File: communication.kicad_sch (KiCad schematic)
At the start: 12 parts, among them IC10 nRF52832-QFAA-R7, Y1 32Mhz

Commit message: added footprint for nRF, changed symbol background color, checked connections
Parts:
- removed IC10: nRF52832-QFAA-R7, QFN40P600X600X90-49N-D, symbol ARMband:nRF52832-QFAA-R7
- added IC11: nRF52832-QFAA-R7, QFN40P600X600X90-49N-D, symbol ARMband:nRF52832-QFAA-R7
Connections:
- net ANT: now also IC11.30 (ANT)
- net BUCK4_1V8: now also IC11.13 (VDD_1), IC11.36 (VDD_2), IC11.48 (VDD_3)
- net DCC: now also IC11.47 (DCC)
- net DEC4: now also IC11.46 (DEC4)
- net GND: now also IC11.31 (VSS_1), IC11.45 (VSS_2), IC11.49 (THERMAL_PAD)
- net nRF_XC1: now also IC11.34 (XC1)
- net nRF_XC2: now also IC11.35 (XC2)
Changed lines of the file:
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@@
     )
   )
-  (symbol (lib_id "ARMband:nRF52832-QFAA-R7") (at 43.18 73.66 0) (unit 1)
+  (symbol (lib_id "Device:L_Small") (at 121.92 69.85 90) (unit 1)
     (in_bom yes) (on_board yes) (dnp no) (fields_autoplaced)
-    (property "Reference" "IC10" (at 57.8359 136.2917 0)
+    (property "Reference" "L8" (at 121.92 66.4613 90)
+      (effects (font (size 1.27 1.27)))
+    )
+    (property "Value" "3.9nH" (at 121.92 68.3823 90)
+      (effects (font (size 1.27 1.27)))
+    )
+    (property "Footprint" "" (at 121.92 69.85 0)
+      (effects (font (size 1.27 1.27)) hide)
+    )
+    (property "Datasheet" "~" (at 121.92 69.85 0)
+      (effects (font (size 1.27 1.27)) hide)
+    )
+    (pin "1")
+    (pin "2")
+    (instances
+      (project "gba"
+        (path "/017c50c6-333c-4d31-ad5a-278994a09b14/647ca51e-1670-44f9-a82c-44b1c60d10f9"
+          (reference "L8") (unit 1)
+        )
+      )
+    )
+  )
+  (symbol (lib_id "Device:C_Small") (at 119.38 54.61 0) (unit 1)
+    (in_bom yes) (on_board yes) (dnp no)
+    (property "Reference" "C69" (at 125.73 55.88 0)
+      (effects (font (size 1.27 1.27)) (justify right))
+    )
+    (property "Value" "100nF" (at 125.73 53.34 0)
+      (effects (font (size 1.27 1.27)) (justify right))
+    )
+    (property "Footprint" "" (at 119.38 54.61 0)
+      (effects (font (size 1.27 1.27)) hide)
+    )
+    (property "Datasheet" "~" (at 119.38 54.61 0)
+      (effects (font (size 1.27 1.27)) hide)
+    )
+    (pin "1")
+    (pin "2")
+    (instances
+      (project "gba"
+        (path "/017c50c6-333c-4d31-ad5a-278994a09b14/647ca51e-1670-44f9-a82c-44b1c60d10f9"
+          (reference "C69") (unit 1)
+        )
+      )
+    )
+  )
+  (symbol (lib_id "Device:L_Small") (at 147.32 52.07 180) (unit 1)
+    (in_bom yes) (on_board yes) (dnp no) (fields_autoplaced)
+    (property "Reference" "L7" (at 147.955 51.4263 0)
+      (effects (font (size 1.27 1.27)) (justify right))
+    )
+    (property "Value" "10uH" (at 147.955 53.3473 0)
+      (effects (font (size 1.27 1.27)) (justify right))
+    )
+    (property "Footprint" "" (at 147.32 52.07 0)
+      (effects (font (size 1.27 1.27)) hide)
+    )
+    (property "Datasheet" "~" (at 147.32 52.07 0)
+      (effects (font (size 1.27 1.27)) hide)
+    )
+    (pin "1")
+    (pin "2")
+    (instances
+      (project "gba"
+        (path "/017c50c6-333c-4d31-ad5a-278994a09b14/647ca51e-1670-44f9-a82c-44b1c60d10f9"
+          (reference "L7") (unit 1)
+        )
+      )
+    )
+  )
+  (symbol (lib_name "nRF52832-QFAA-R7_1") (lib_id "ARMband:nRF52832-QFAA-R7") (at 43.18 73.66 0) (unit 1)
+    (in_bom yes) (on_board yes) (dnp no) (fields_autoplaced)
+    (property "Reference" "IC11" (at 57.8359 137.16 0)
       (effects (font (size 1.27 1.27)) (justify left))
     )
-    (property "Value" "nRF52832-QFAA-R7" (at 57.8359 138.2127 0)
+    (property "Value" "nRF52832-QFAA-R7" (at 57.8359 139.7 0)
       (effects (font (size 1.27 1.27)) (justify left))
     )
@@
       (project "gba"
         (path "/017c50c6-333c-4d31-ad5a-278994a09b14/647ca51e-1670-44f9-a82c-44b1c60d10f9"
-          (reference "IC10") (unit 1)
+          (reference "IC11") (unit 1)
         )
       )
-    )
-  )
-  (symbol (lib_id "Device:L_Small") (at 121.92 69.85 90) (unit 1)
-    (in_bom yes) (on_board yes) (dnp no) (fields_autoplaced)
-    (property "Reference" "L8" (at 121.92 66.4613 90)
-      (effects (font (size 1.27 1.27)))
-    )
-    (property "Value" "3.9nH" (at 121.92 68.3823 90)
-      (effects (font (size 1.27 1.27)))
-    )
-    (property "Footprint" "" (at 121.92 69.85 0)
-      (effects (font (size 1.27 1.27)) hide)
-    )
-    (property "Datasheet" "~" (at 121.92 69.85 0)
-      (effects (font (size 1.27 1.27)) hide)
-    )
-    (pin "1")
-    (pin "2")
-    (instances
-      (project "gba"
-        (path "/017c50c6-333c-4d31-ad5a-278994a09b14/647ca51e-1670-44f9-a82c-44b1c60d10f9"
-          (reference "L8") (unit 1)
-        )
-      )
-    )
-  )
-  (symbol (lib_id "Device:C_Small") (at 119.38 54.61 0) (unit 1)
-    (in_bom yes) (on_board yes) (dnp no)
-    (property "Reference" "C69" (at 125.73 55.88 0)
-      (effects (font (size 1.27 1.27)) (justify right))
-    )
-    (property "Value" "100nF" (at 125.73 53.34 0)
-      (effects (font (size 1.27 1.27)) (justify right))
-    )
-    (property "Footprint" "" (at 119.38 54.61 0)
-      (effects (font (size 1.27 1.27)) hide)
-    )
-    (property "Datasheet" "~" (at 119.38 54.61 0)
-      (effects (font (size 1.27 1.27)) hide)
-    )
-    (pin "1")
-    (pin "2")
-    (instances
-      (project "gba"
-        (path "/017c50c6-333c-4d31-ad5a-278994a09b14/647ca51e-1670-44f9-a82c-44b1c60d10f9"
-          (reference "C69") (unit 1)
-        )
-      )
-    )
-  )
-  (symbol (lib_id "Device:L_Small") (at 147.32 52.07 180) (unit 1)
-    (in_bom yes) (on_board yes) (dnp no) (fields_autoplaced)
-    (property "Reference" "L7" (at 147.955 51.4263 0)
-      (effects (font (size 1.27 1.27)) (justify right))
-    )
-    (property "Value" "10uH" (at 147.955 53.3473 0)
-      (effects (font (size 1.27 1.27)) (justify right))
-    )
-    (property "Footprint" "" (at 147.32 52.07 0)
-      (effects (font (size 1.27 1.27)) hide)
-    )
-    (property "Datasheet" "~" (at 147.32 52.07 0)
-      (effects (font (size 1.27 1.27)) hide)
-    )
-    (pin "1")
-    (pin "2")
-    (instances
-      (project "gba"
-        (path "/017c50c6-333c-4d31-ad5a-278994a09b14/647ca51e-1670-44f9-a82c-44b1c60d10f9"
-          (reference "L7") (unit 1)
-        )
-      )

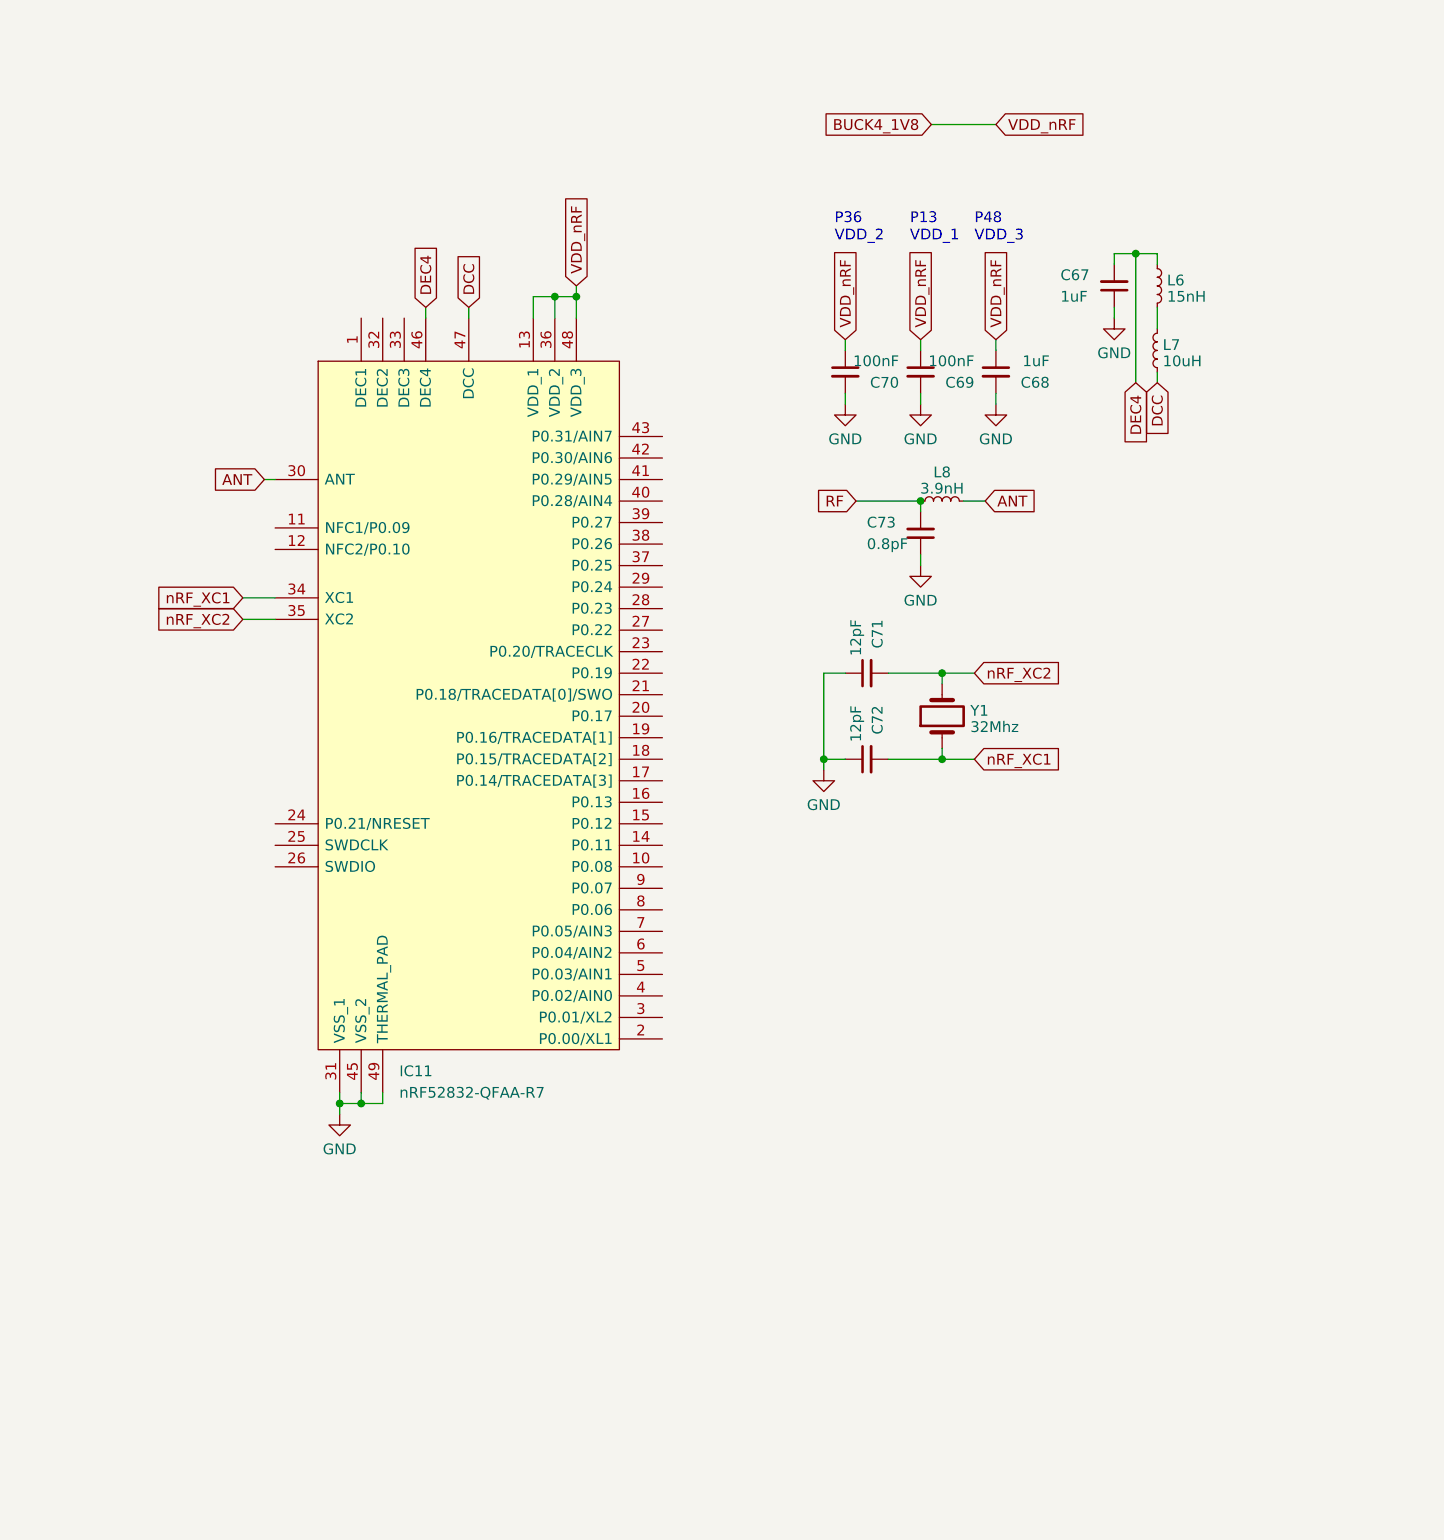
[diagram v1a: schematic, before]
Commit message: added supply to nRF
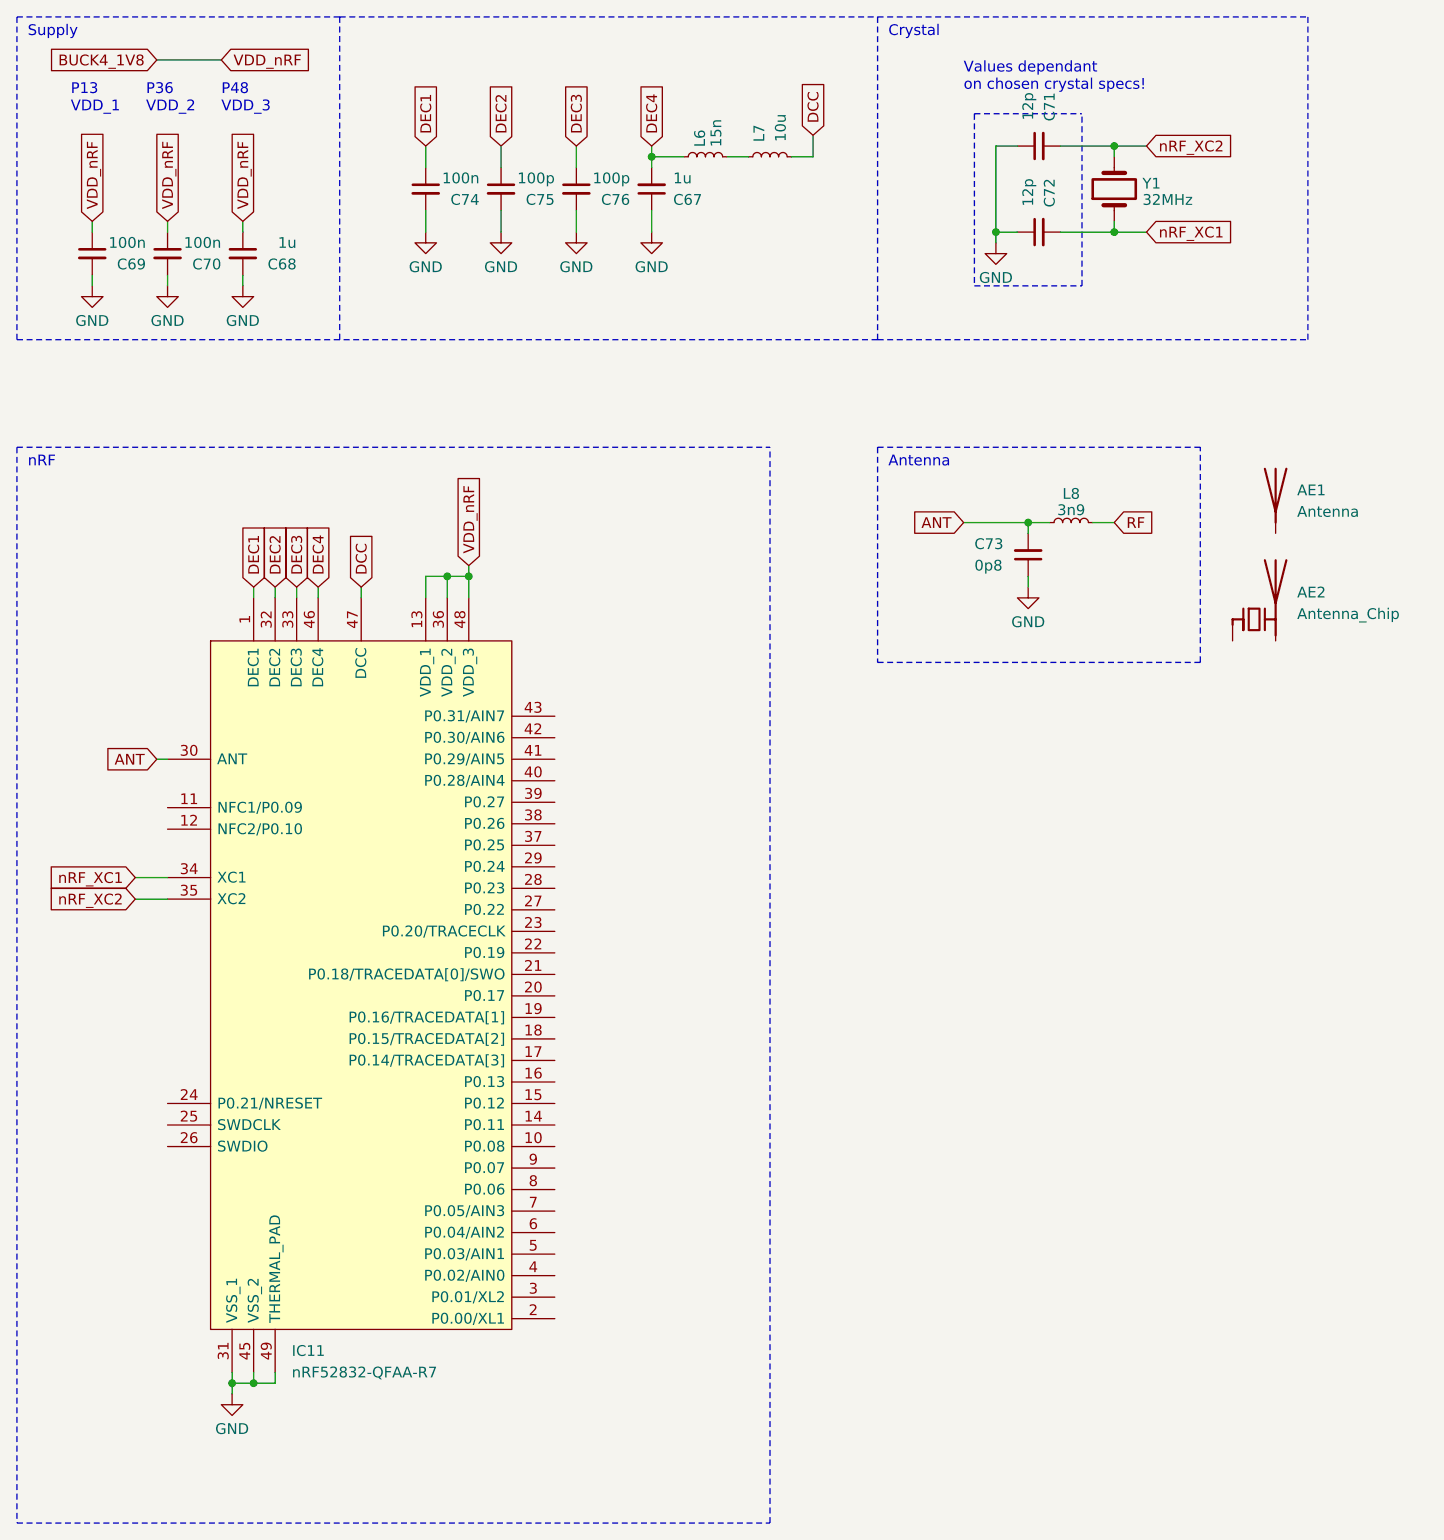
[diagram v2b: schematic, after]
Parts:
- added AE1: Antenna, symbol Device:Antenna
- added AE2: Antenna_Chip, symbol Device:Antenna_Chip
- added C74: 100n, symbol Device:C_Small
- added C75, C76: 100p, symbol Device:C_Small
- C67, C68: value 1uF -> 1u
- C69, C70: value 100nF -> 100n
- C71, C72: value 12pF -> 12p
- C73: value 0.8pF -> 0p8
- L6: value 15nH -> 15n
- L7: value 10uH -> 10u
- L8: value 3.9nH -> 3n9
- Y1: value 32Mhz -> 32MHz
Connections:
- net ANT: now also C73.2, L8.1; no longer L8.2
- net DCC: now also L7.2; no longer L7.1
- net GND: now also C74.2, C75.2, C76.2
- net RF: now also L8.2; no longer C73.2, L8.1
- net at L6.2: now also L7.1; no longer L7.2
- net DEC1: now reaches IC11.1 (DEC1)
- net DEC1: now also C74.1
- net DEC2: now reaches IC11.32 (DEC2)
- net DEC2: now also C75.1
- net DEC3: now reaches IC11.33 (DEC3)
- net DEC3: now also C76.1
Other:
- note added: "Antenna"
- note added: "Crystal"
- note added: "Supply"
- note added: "Values dependant on chosen crystal specs!"
- note added: "nRF"
- moved on the sheet: C67, C68, C69, C70, C71, C72, C73, IC11, L6, L7, L8, Y1

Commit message: added decoupling capacitors to mp1
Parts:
- C68: value 1u -> 4u7
- C75: now not fitted
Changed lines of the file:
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@@
       (effects (font (size 1.27 1.27)) (justify right))
     )
-    (property "Value" "1u" (at 45.72 39.37 0)
+    (property "Value" "4u7" (at 45.72 39.37 0)
       (effects (font (size 1.27 1.27)) (justify right))
     )
@@
     )
     (property "Datasheet" "~" (at 39.37 40.64 0)
+      (effects (font (size 1.27 1.27)) hide)
+    )
+    (property "MFN" "" (at 39.37 40.64 0)
       (effects (font (size 1.27 1.27)) hide)
     )
@@
   )
   (symbol (lib_id "Device:C_Small") (at 69.85 33.02 0) (unit 1)
-    (in_bom yes) (on_board yes) (dnp no)
+    (in_bom yes) (on_board yes) (dnp yes)
     (property "Reference" "C75" (at 76.2 34.29 0)
       (effects (font (size 1.27 1.27)) (justify right))
